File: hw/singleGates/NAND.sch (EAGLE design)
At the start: 5 parts, among them Q1 BC817, Q2 BC817

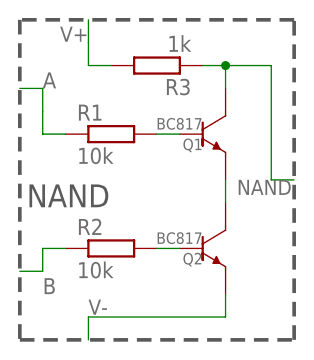
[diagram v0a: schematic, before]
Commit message: Updated supply line names to be more spice compatible
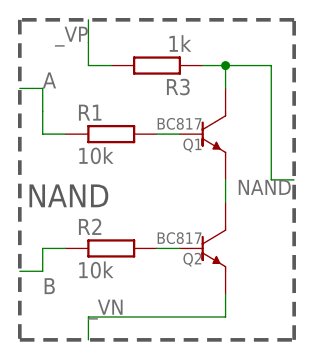
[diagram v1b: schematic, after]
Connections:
- net V+ renamed _VP
- net V- renamed _VN
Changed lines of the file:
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@@
 <?xml version="1.0" encoding="utf-8"?>
 <!DOCTYPE eagle SYSTEM "eagle.dtd">
-<eagle version="7.4.0">
+<eagle version="7.3.0">
 <drawing>
 <settings>
@@
 </segment>
 </net>
-<net name="V+" class="0">
+<net name="_VP" class="0">
 <segment>
 <pinref part="R3" gate="G$1" pin="2"/>
@@
 </segment>
 </net>
-<net name="V-" class="0">
+<net name="_VN" class="0">
 <segment>
 <wire x1="-7.62" y1="-17.78" x2="-7.62" y2="-15.24" width="0.1524" layer="91"/>
